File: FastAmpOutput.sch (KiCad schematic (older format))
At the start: 20 parts

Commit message: Schematic complete (mostly, may have bugs) initial layout of parts on pcb, no connecting bits
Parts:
- added C205, C206, C207, C208: 2400pF, SM1206, symbol C
- C201, C202, C203, C204: renamed from C?; footprint ~ -> SM1206
- R201, R202, R203, R204, R205, R206, R207, R208: renamed from R?; footprint ~ -> SM1206
- gave numbers to parts that had none: 8
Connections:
- net +12V: now reaches R205.1
- net +12V: now also R206.1, R207.1, R208.1
- net at R205.2: now also R201.1
- net at R201.2: now also U201.5 (DC)
- net at U201.2 (RF-IN,DC): now also Q201.3 (DC/RF), C205.1
- net at Q201.1 (RF-IN): now also C201.1
- net GND: now reaches Q201.2 (GND)
- net GND: now also Q201.4 (GND), Q202.2 (GND), Q202.4 (GND), Q203.2 (GND), Q203.4 (GND), Q204.2 (GND), Q204.4 (GND)
- net Amplifier1_Input: now reaches C201.2
- net at R206.2: now also R202.1
- net at R202.2: now also U202.5 (DC)
- net at U202.2 (RF-IN,DC): now also Q202.3 (DC/RF), C206.1
- net at Q202.1 (RF-IN): now also C202.1
- net Amplifier2_Input: now reaches C202.2
- net at R207.2: now also R203.1
- net at R203.2: now also U203.5 (DC)
- net at U203.2 (RF-IN,DC): now also Q203.3 (DC/RF), C207.1
- net at Q203.1 (RF-IN): now also C203.1
- net Amplifier3_Input: now reaches C203.2
- net at R208.2: now also R204.1
- net at R204.2: now also U204.5 (DC)
- net at U204.2 (RF-IN,DC): now also Q204.3 (DC/RF), C208.1
- net at Q204.1 (RF-IN): now also C204.1
- net Amplifier4_Input: now reaches C204.2
- new net Amplifier1_Output: C205.2
- new net Amplifier2_Output: C206.2
- new net Amplifier3_Output: C207.2
- new net Amplifier4_Output: C208.2
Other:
- moved on the sheet: C201, C202, C203, C204, Q201, Q202, Q203, Q204

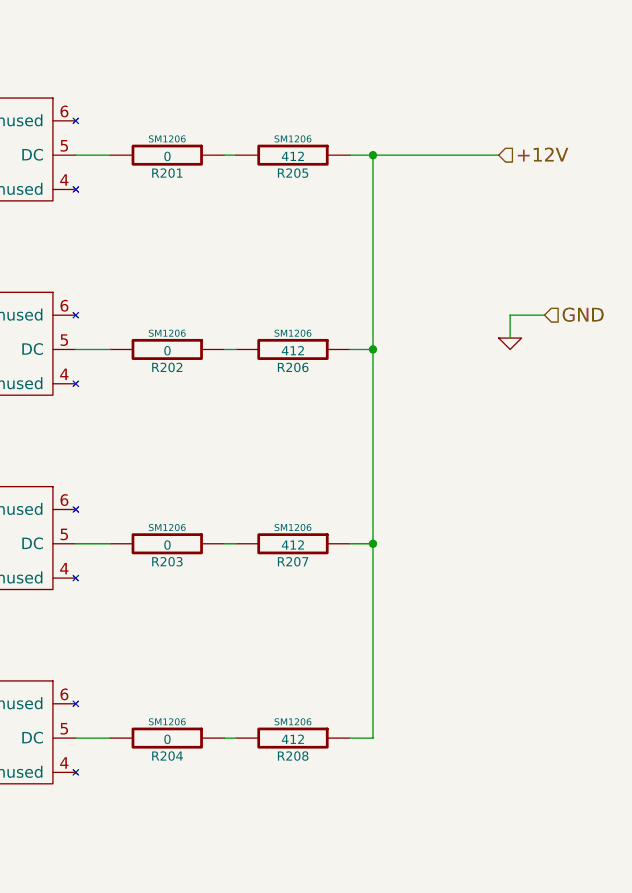
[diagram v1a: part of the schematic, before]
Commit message: Schematic has been pretty much finished, on the pcb layout I've got everything positioned in a "this will probably work" kind of setup (it has much potential for improvement). Next up, routing the lines, I think I can get this done on 4 layers, although for signal integrity six would work better.
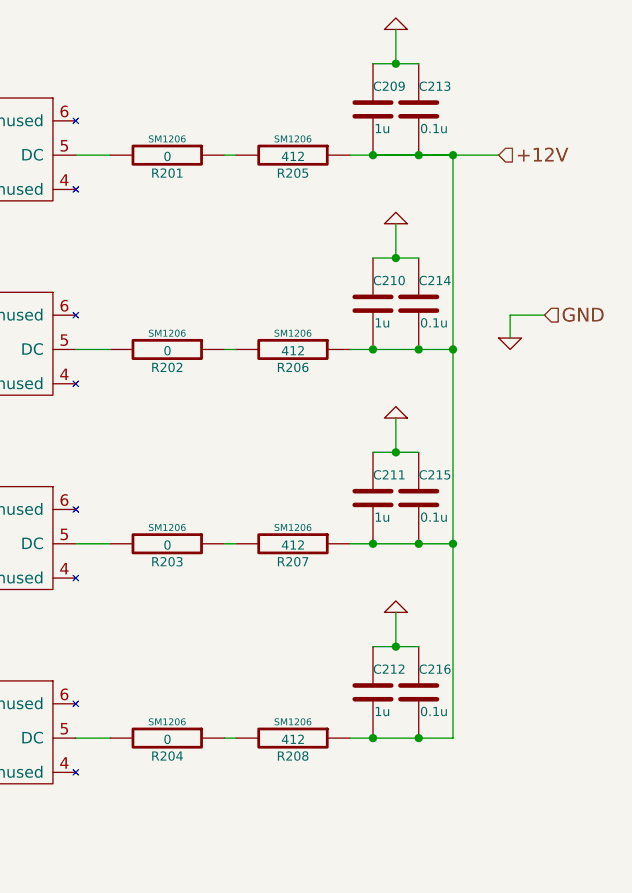
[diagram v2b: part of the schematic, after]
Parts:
- added C209, C210, C211, C212: 1u, ~, symbol C
- added C213, C214, C215, C216: 0.1u, ~, symbol C
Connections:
- net +12V: now also C209.2, C210.2, C211.2, C212.2, C213.2, C214.2, C215.2, C216.2
- net GND: now also C209.1, C210.1, C211.1, C212.1, C213.1, C214.1, C215.1, C216.1
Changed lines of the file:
@@
 Sheet 2 2
 Title ""
-Date "18 jun 2014"
+Date "20 jun 2014"
 Rev ""
 Comp ""
@@
 	6650 1650 6000 1650
 Wire Wire Line
-	6100 1650 6100 4200
-Wire Wire Line
-	6100 2500 6000 2500
-Connection ~ 6100 1650
-Wire Wire Line
-	6100 3350 6000 3350
-Connection ~ 6100 2500
-Wire Wire Line
-	6100 4200 6000 4200
-Connection ~ 6100 3350
+	6000 2500 6450 2500
+Wire Wire Line
+	6450 3350 6000 3350
+Wire Wire Line
+	6450 4200 6000 4200
 Wire Wire Line
 	5500 4200 5450 4200
@@
 Connection ~ 3450 3350
 Connection ~ 3450 4200
+$Comp
+L C C209
+U 1 1 53A4516D
+P 6100 1450
+F 0 "C209" H 6100 1550 40  0000 L CNN
+F 1 "1u" H 6106 1365 40  0000 L CNN
+F 2 "~" H 6138 1300 30  0000 C CNN
+F 3 "~" H 6100 1450 60  0000 C CNN
+	1    6100 1450
+	1    0    0    -1
+$EndComp
+$Comp
+L C C213
+U 1 1 53A4517C
+P 6300 1450
+F 0 "C213" H 6300 1550 40  0000 L CNN
+F 1 "0.1u" H 6306 1365 40  0000 L CNN
+F 2 "~" H 6338 1300 30  0000 C CNN
+F 3 "~" H 6300 1450 60  0000 C CNN
+	1    6300 1450
+	1    0    0    -1
+$EndComp
+$Comp
+L C C210
+U 1 1 53A4518B
+P 6100 2300
+F 0 "C210" H 6100 2400 40  0000 L CNN
+F 1 "1u" H 6106 2215 40  0000 L CNN
+F 2 "~" H 6138 2150 30  0000 C CNN
+F 3 "~" H 6100 2300 60  0000 C CNN
+	1    6100 2300
+	1    0    0    -1
+$EndComp
+$Comp
+L C C214
+U 1 1 53A4519A
+P 6300 2300
+F 0 "C214" H 6300 2400 40  0000 L CNN
+F 1 "0.1u" H 6306 2215 40  0000 L CNN
+F 2 "~" H 6338 2150 30  0000 C CNN
+F 3 "~" H 6300 2300 60  0000 C CNN
+	1    6300 2300
+	1    0    0    -1
+$EndComp
+$Comp
+L C C211
+U 1 1 53A451A9
+P 6100 3150
+F 0 "C211" H 6100 3250 40  0000 L CNN
+F 1 "1u" H 6106 3065 40  0000 L CNN
+F 2 "~" H 6138 3000 30  0000 C CNN
+F 3 "~" H 6100 3150 60  0000 C CNN
+	1    6100 3150
+	1    0    0    -1
+$EndComp
+$Comp
+L C C215
+U 1 1 53A451B8
+P 6300 3150
+F 0 "C215" H 6300 3250 40  0000 L CNN
+F 1 "0.1u" H 6306 3065 40  0000 L CNN
+F 2 "~" H 6338 3000 30  0000 C CNN
+F 3 "~" H 6300 3150 60  0000 C CNN
+	1    6300 3150
+	1    0    0    -1
+$EndComp
+$Comp
+L C C212
+U 1 1 53A451C7
+P 6100 4000
+F 0 "C212" H 6100 4100 40  0000 L CNN
+F 1 "1u" H 6106 3915 40  0000 L CNN
+F 2 "~" H 6138 3850 30  0000 C CNN
+F 3 "~" H 6100 4000 60  0000 C CNN
+	1    6100 4000
+	1    0    0    -1
+$EndComp
+$Comp
+L C C216
+U 1 1 53A451D6
+P 6300 4000
+F 0 "C216" H 6300 4100 40  0000 L CNN
+F 1 "0.1u" H 6306 3915 40  0000 L CNN
+F 2 "~" H 6338 3850 30  0000 C CNN
+F 3 "~" H 6300 4000 60  0000 C CNN
+	1    6300 4000
+	1    0    0    -1
+$EndComp
+Connection ~ 6100 2500
+Connection ~ 6100 3350
+Connection ~ 6100 4200
+$Comp
+L GND #PWR021
+U 1 1 53A4529A
+P 6200 3650
+F 0 "#PWR021" H 6200 3650 30  0001 C CNN
+F 1 "GND" H 6200 3580 30  0001 C CNN
+F 2 "" H 6200 3650 60  0000 C CNN
+F 3 "" H 6200 3650 60  0000 C CNN
+	1    6200 3650
+	-1   0    0    1
+$EndComp
+$Comp
+L GND #PWR022
+U 1 1 53A452A9
+P 6200 2800
+F 0 "#PWR022" H 6200 2800 30  0001 C CNN
+F 1 "GND" H 6200 2730 30  0001 C CNN
+F 2 "" H 6200 2800 60  0000 C CNN
+F 3 "" H 6200 2800 60  0000 C CNN
+	1    6200 2800
+	-1   0    0    1
+$EndComp
+$Comp
+L GND #PWR023
+U 1 1 53A452B8
+P 6200 1950
+F 0 "#PWR023" H 6200 1950 30  0001 C CNN
+F 1 "GND" H 6200 1880 30  0001 C CNN
+F 2 "" H 6200 1950 60  0000 C CNN
+F 3 "" H 6200 1950 60  0000 C CNN
+	1    6200 1950
+	-1   0    0    1
+$EndComp
+$Comp
+L GND #PWR024
+U 1 1 53A452C7
+P 6200 1100
+F 0 "#PWR024" H 6200 1100 30  0001 C CNN
+F 1 "GND" H 6200 1030 30  0001 C CNN
+F 2 "" H 6200 1100 60  0000 C CNN
+F 3 "" H 6200 1100 60  0000 C CNN
+	1    6200 1100
+	-1   0    0    1
+$EndComp
+Wire Wire Line
+	6100 1250 6300 1250
+Wire Wire Line
+	6200 1250 6200 1100
+Connection ~ 6200 1250
+Wire Wire Line
+	6200 1950 6200 2100
+Wire Wire Line
+	6100 2100 6300 2100
+Connection ~ 6200 2100
+Wire Wire Line
+	6100 2950 6300 2950
+Wire Wire Line
+	6200 2950 6200 2800
+Connection ~ 6200 2950
+Wire Wire Line
+	6100 3800 6300 3800
+Wire Wire Line
+	6200 3800 6200 3650
+Connection ~ 6200 3800
+Wire Wire Line
+	6450 1650 6450 4200
+Connection ~ 6300 2500
+Connection ~ 6450 1650
+Connection ~ 6300 3350
+Connection ~ 6450 2500
+Connection ~ 6300 4200
+Connection ~ 6450 3350
+Wire Wire Line
+	6100 1650 6450 1650
+Connection ~ 6300 1650
+Connection ~ 6100 1650
 $EndSCHEMATC

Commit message: Combined GND and COMM_N into just COMM_N, have everything connected and space a little minimized. I have an idea I'd like to try. If I increase the board layers I think I can move the Amplifier section on top of the actual pass-through lines which would save a lot of space at the cost of rework and increased manufacturing cost / sq in.
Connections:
- net GND renamed COMM_N
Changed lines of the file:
@@
 Sheet 2 2
 Title ""
-Date "30 jun 2014"
+Date "2 jul 2014"
 Rev ""
 Comp ""
@@
 Wire Wire Line
 	3150 4200 3800 4200
-$Comp
-L GND #PWR023
-U 1 1 538F450B
-P 2600 2050
-F 0 "#PWR023" H 2600 2050 30  0001 C CNN
-F 1 "GND" H 2600 1980 30  0001 C CNN
-F 2 "" H 2600 2050 60  0000 C CNN
-F 3 "" H 2600 2050 60  0000 C CNN
-	1    2600 2050
-	0    1    1    0
-$EndComp
-$Comp
-L GND #PWR024
-U 1 1 538F451A
-P 2550 2900
-F 0 "#PWR024" H 2550 2900 30  0001 C CNN
-F 1 "GND" H 2550 2830 30  0001 C CNN
-F 2 "" H 2550 2900 60  0000 C CNN
-F 3 "" H 2550 2900 60  0000 C CNN
-	1    2550 2900
-	0    1    1    0
-$EndComp
-$Comp
-L GND #PWR025
-U 1 1 538F4529
-P 2550 3800
-F 0 "#PWR025" H 2550 3800 30  0001 C CNN
-F 1 "GND" H 2550 3730 30  0001 C CNN
-F 2 "" H 2550 3800 60  0000 C CNN
-F 3 "" H 2550 3800 60  0000 C CNN
-	1    2550 3800
-	0    1    1    0
-$EndComp
 Wire Wire Line
 	2600 2050 2800 2050
@@
 	2800 3700 2800 3850
 Connection ~ 2800 3800
-$Comp
-L GND #PWR026
-U 1 1 538F4622
-P 2800 4750
-F 0 "#PWR026" H 2800 4750 30  0001 C CNN
-F 1 "GND" H 2800 4680 30  0001 C CNN
-F 2 "" H 2800 4750 60  0000 C CNN
-F 3 "" H 2800 4750 60  0000 C CNN
-	1    2800 4750
-	1    0    0    -1
-$EndComp
-$Comp
-L GND #PWR027
-U 1 1 538F4631
-P 2800 1100
-F 0 "#PWR027" H 2800 1100 30  0001 C CNN
-F 1 "GND" H 2800 1030 30  0001 C CNN
-F 2 "" H 2800 1100 60  0000 C CNN
-F 3 "" H 2800 1100 60  0000 C CNN
-	1    2800 1100
-	-1   0    0    1
-$EndComp
 Wire Wire Line
 	2800 1100 2800 1300
@@
 	3450 2050 3600 2050
 Text HLabel 6850 2350 2    60   Input ~ 0
-GND
-$Comp
-L GND #PWR028
-U 1 1 53A1C66B
-P 6700 2450
-F 0 "#PWR028" H 6700 2450 30  0001 C CNN
-F 1 "GND" H 6700 2380 30  0001 C CNN
-F 2 "" H 6700 2450 60  0000 C CNN
-F 3 "" H 6700 2450 60  0000 C CNN
-	1    6700 2450
-	1    0    0    -1
-$EndComp
+COMM_N
 Wire Wire Line
 	6850 2350 6700 2350
@@
 Connection ~ 6100 3350
 Connection ~ 6100 4200
-$Comp
-L GND #PWR029
-U 1 1 53A4529A
-P 6200 3650
-F 0 "#PWR029" H 6200 3650 30  0001 C CNN
-F 1 "GND" H 6200 3580 30  0001 C CNN
-F 2 "" H 6200 3650 60  0000 C CNN
-F 3 "" H 6200 3650 60  0000 C CNN
-	1    6200 3650
-	-1   0    0    1
-$EndComp
-$Comp
-L GND #PWR030
-U 1 1 53A452A9
-P 6200 2800
-F 0 "#PWR030" H 6200 2800 30  0001 C CNN
-F 1 "GND" H 6200 2730 30  0001 C CNN
-F 2 "" H 6200 2800 60  0000 C CNN
-F 3 "" H 6200 2800 60  0000 C CNN
-	1    6200 2800
-	-1   0    0    1
-$EndComp
-$Comp
-L GND #PWR031
-U 1 1 53A452B8
-P 6200 1950
-F 0 "#PWR031" H 6200 1950 30  0001 C CNN
-F 1 "GND" H 6200 1880 30  0001 C CNN
-F 2 "" H 6200 1950 60  0000 C CNN
-F 3 "" H 6200 1950 60  0000 C CNN
-	1    6200 1950
-	-1   0    0    1
-$EndComp
-$Comp
-L GND #PWR032
-U 1 1 53A452C7
-P 6200 1100
-F 0 "#PWR032" H 6200 1100 30  0001 C CNN
-F 1 "GND" H 6200 1030 30  0001 C CNN
-F 2 "" H 6200 1100 60  0000 C CNN
-F 3 "" H 6200 1100 60  0000 C CNN
-	1    6200 1100
-	-1   0    0    1
-$EndComp
 Wire Wire Line
 	6100 1250 6300 1250
@@
 Connection ~ 6300 1650
 Connection ~ 6100 1650
+$Comp
+L COMM_N #PWR021
+U 1 1 53B41A10
+P 2800 4750
+F 0 "#PWR021" H 2800 4850 60  0001 C CNN
+F 1 "COMM_N" H 2800 4600 60  0000 C CNN
+F 2 "~" H 2800 4750 60  0000 C CNN
+F 3 "~" H 2800 4750 60  0000 C CNN
+	1    2800 4750
+	1    0    0    -1
+$EndComp
+$Comp
+L COMM_N #PWR022
+U 1 1 53B41A1F
+P 2550 3800
+F 0 "#PWR022" H 2550 3900 60  0001 C CNN
+F 1 "COMM_N" H 2550 3650 60  0000 C CNN
+F 2 "~" H 2550 3800 60  0000 C CNN
+F 3 "~" H 2550 3800 60  0000 C CNN
+	1    2550 3800
+	0    1    1    0
+$EndComp
+$Comp
+L COMM_N #PWR023
+U 1 1 53B41A2E
+P 2550 2900
+F 0 "#PWR023" H 2550 3000 60  0001 C CNN
+F 1 "COMM_N" H 2550 2750 60  0000 C CNN
+F 2 "~" H 2550 2900 60  0000 C CNN
+F 3 "~" H 2550 2900 60  0000 C CNN
+	1    2550 2900
+	0    1    1    0
+$EndComp
+$Comp
+L COMM_N #PWR024
+U 1 1 53B41A3D
+P 2600 2050
+F 0 "#PWR024" H 2600 2150 60  0001 C CNN
+F 1 "COMM_N" H 2600 1900 60  0000 C CNN
+F 2 "~" H 2600 2050 60  0000 C CNN
+F 3 "~" H 2600 2050 60  0000 C CNN
+	1    2600 2050
+	0    1    1    0
+$EndComp
+$Comp
+L COMM_N #PWR025
+U 1 1 53B41A4C
+P 2800 1100
+F 0 "#PWR025" H 2800 1200 60  0001 C CNN
+F 1 "COMM_N" H 2800 950 60  0000 C CNN
+F 2 "~" H 2800 1100 60  0000 C CNN
+F 3 "~" H 2800 1100 60  0000 C CNN
+	1    2800 1100
+	-1   0    0    1
+$EndComp
+$Comp
+L COMM_N #PWR026
+U 1 1 53B41A5B
+P 6700 2450
+F 0 "#PWR026" H 6700 2550 60  0001 C CNN
+F 1 "COMM_N" H 6700 2300 60  0000 C CNN
+F 2 "~" H 6700 2450 60  0000 C CNN
+F 3 "~" H 6700 2450 60  0000 C CNN
+	1    6700 2450
+	1    0    0    -1
+$EndComp
+$Comp
+L COMM_N #PWR027
+U 1 1 53B41A6A
+P 6200 3650
+F 0 "#PWR027" H 6200 3750 60  0001 C CNN
+F 1 "COMM_N" H 6200 3500 60  0000 C CNN
+F 2 "~" H 6200 3650 60  0000 C CNN
+F 3 "~" H 6200 3650 60  0000 C CNN
+	1    6200 3650
+	-1   0    0    1
+$EndComp
+$Comp
+L COMM_N #PWR028
+U 1 1 53B41A79
+P 6200 2800
+F 0 "#PWR028" H 6200 2900 60  0001 C CNN
+F 1 "COMM_N" H 6200 2650 60  0000 C CNN
+F 2 "~" H 6200 2800 60  0000 C CNN
+F 3 "~" H 6200 2800 60  0000 C CNN
+	1    6200 2800
+	-1   0    0    1
+$EndComp
+$Comp
+L COMM_N #PWR029
+U 1 1 53B41A88
+P 6200 1950
+F 0 "#PWR029" H 6200 2050 60  0001 C CNN
+F 1 "COMM_N" H 6200 1800 60  0000 C CNN
+F 2 "~" H 6200 1950 60  0000 C CNN
+F 3 "~" H 6200 1950 60  0000 C CNN
+	1    6200 1950
+	-1   0    0    1
+$EndComp
+$Comp
+L COMM_N #PWR030
+U 1 1 53B41A97
+P 6200 1100
+F 0 "#PWR030" H 6200 1200 60  0001 C CNN
+F 1 "COMM_N" H 6200 950 60  0000 C CNN
+F 2 "~" H 6200 1100 60  0000 C CNN
+F 3 "~" H 6200 1100 60  0000 C CNN
+	1    6200 1100
+	-1   0    0    1
+$EndComp
 $EndSCHEMATC
